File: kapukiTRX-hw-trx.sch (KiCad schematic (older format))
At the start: 28 parts, among them J1 GPS, J2 SWD, J21 Conn_01x01, J22 Conn_01x01, U1 STM32G474VE, U2 LP38693-3.3, Y1 16MHz

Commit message: Add an elec cap to cup rail
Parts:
- added C41: 10uF, Capacitor_Tantalum_SMD:CP_EIA-3216-18_Kemet-A, symbol Device:CP
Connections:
- wire segments 161 -> 165
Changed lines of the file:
@@
 	4950 6300 5150 6300
 Connection ~ 4950 6300
+$Comp
+L Device:CP C41
+U 1 1 5DCE2D86
+P 950 1000
+F 0 "C41" H 1068 1046 50  0000 L CNN
+F 1 "10uF" H 1068 955 50  0000 L CNN
+F 2 "Capacitor_Tantalum_SMD:CP_EIA-3216-18_Kemet-A" H 988 850 50  0001 C CNN
+F 3 "~" H 950 1000 50  0001 C CNN
+	1    950  1000
+	1    0    0    -1
+$EndComp
+Wire Wire Line
+	950  850  950  650
+Wire Wire Line
+	950  650  1400 650
+Connection ~ 1400 650
+Wire Wire Line
+	950  1150 950  1350
+Wire Wire Line
+	950  1350 1400 1350
 $EndSCHEMATC

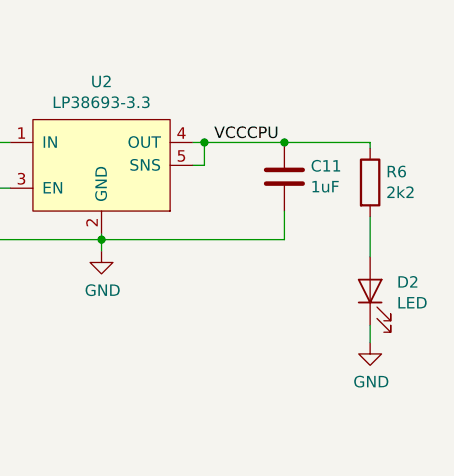
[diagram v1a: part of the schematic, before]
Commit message: Fix BMP388 footprint issue
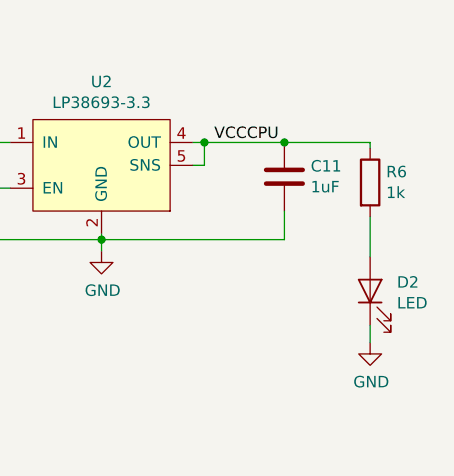
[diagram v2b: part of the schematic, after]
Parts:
- R6: value 2k2 -> 1k
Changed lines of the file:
@@
 EESchema Schematic File Version 4
+LIBS:kapukiTRX-hw-trx-cache
 EELAYER 30 0
 EELAYER END
@@
 P 10800 1275
 F 0 "R6" H 10870 1321 50  0000 L CNN
-F 1 "2k2" H 10870 1230 50  0000 L CNN
+F 1 "1k" H 10870 1230 50  0000 L CNN
 F 2 "Resistor_SMD:R_0402_1005Metric" V 10730 1275 50  0001 C CNN
 F 3 "~" H 10800 1275 50  0001 C CNN

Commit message: Final changes for rev.3
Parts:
- added R15: 0, Resistor_SMD:R_0402_1005Metric, symbol Device:R
- added R16: 10k, Resistor_SMD:R_0402_1005Metric, symbol Device:R
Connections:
- wire segments 165 -> 175
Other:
- note added: "CAN and servo interface"
- note added: "Extra serial port"
- note added: "GPS module connection"
- note added: "Main CPU"
- note added: "Redundant SX1280 RF modules (2.4 GHz)"
- note added: "SWD programming port"
- note added: "Sensors (9-axis absolute orientation sensor & pressure sensor for altitude measurement)"
- note added: "Status LED"
- note added: "Transmitter or receiver selection\nR15 mounter: transmitter\nR15 not mounted: receiver"
- moved on the sheet: C5, D1, J1, J2, J21, J22, R1, R14, R2, R3, R4

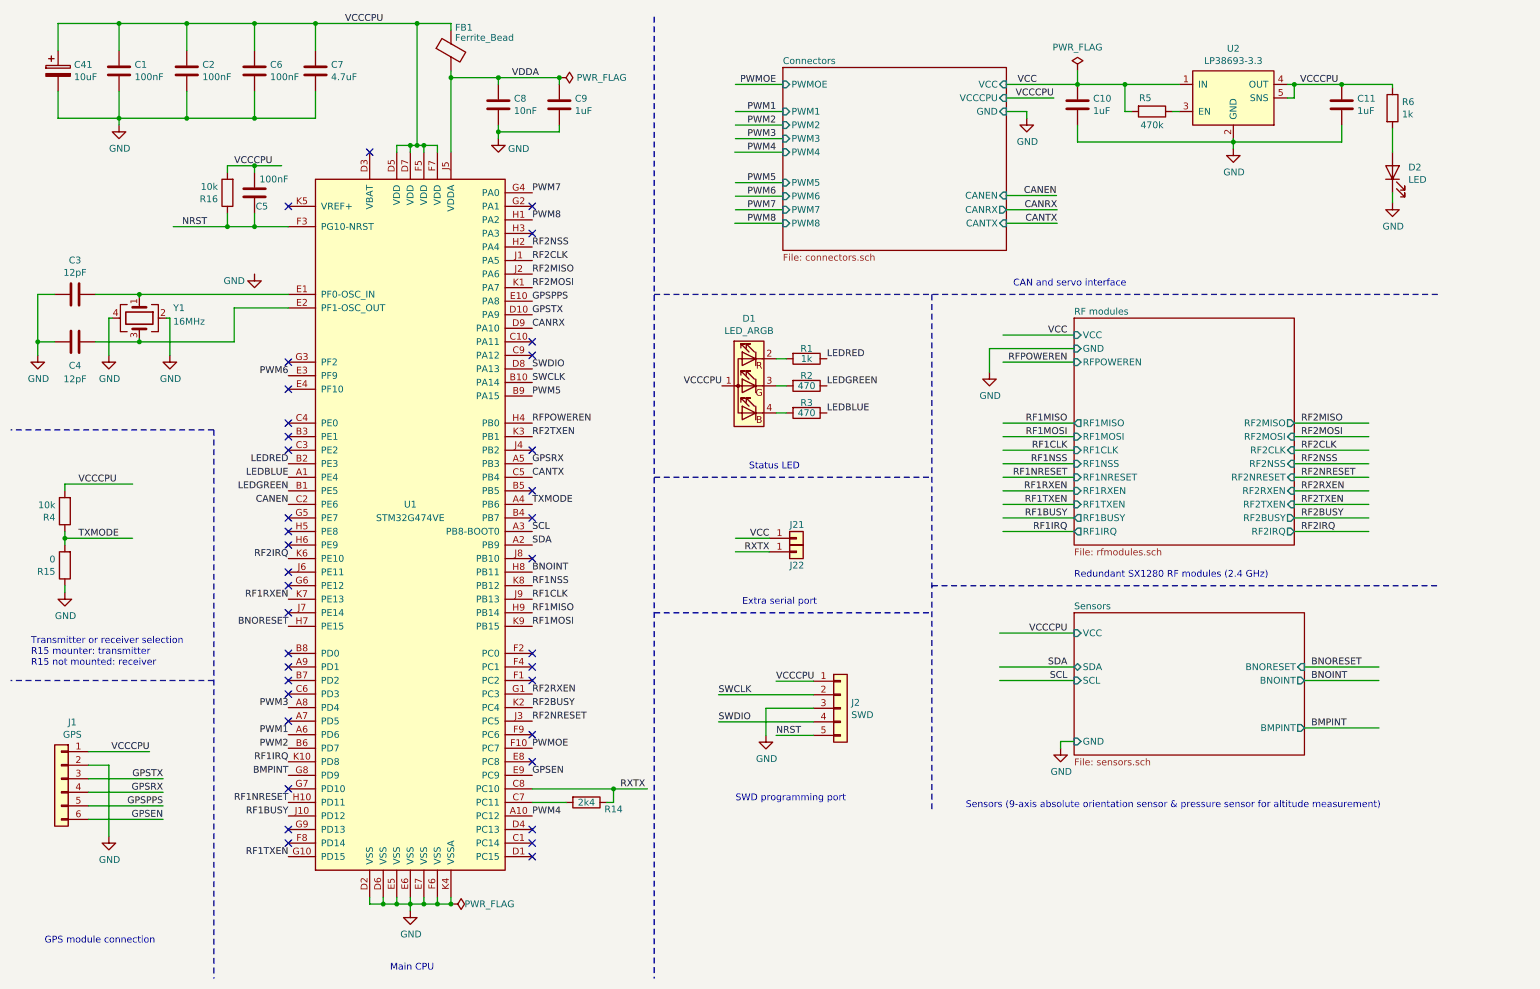
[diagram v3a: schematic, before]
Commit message: Add boot resistor, and fix CAN RX pin
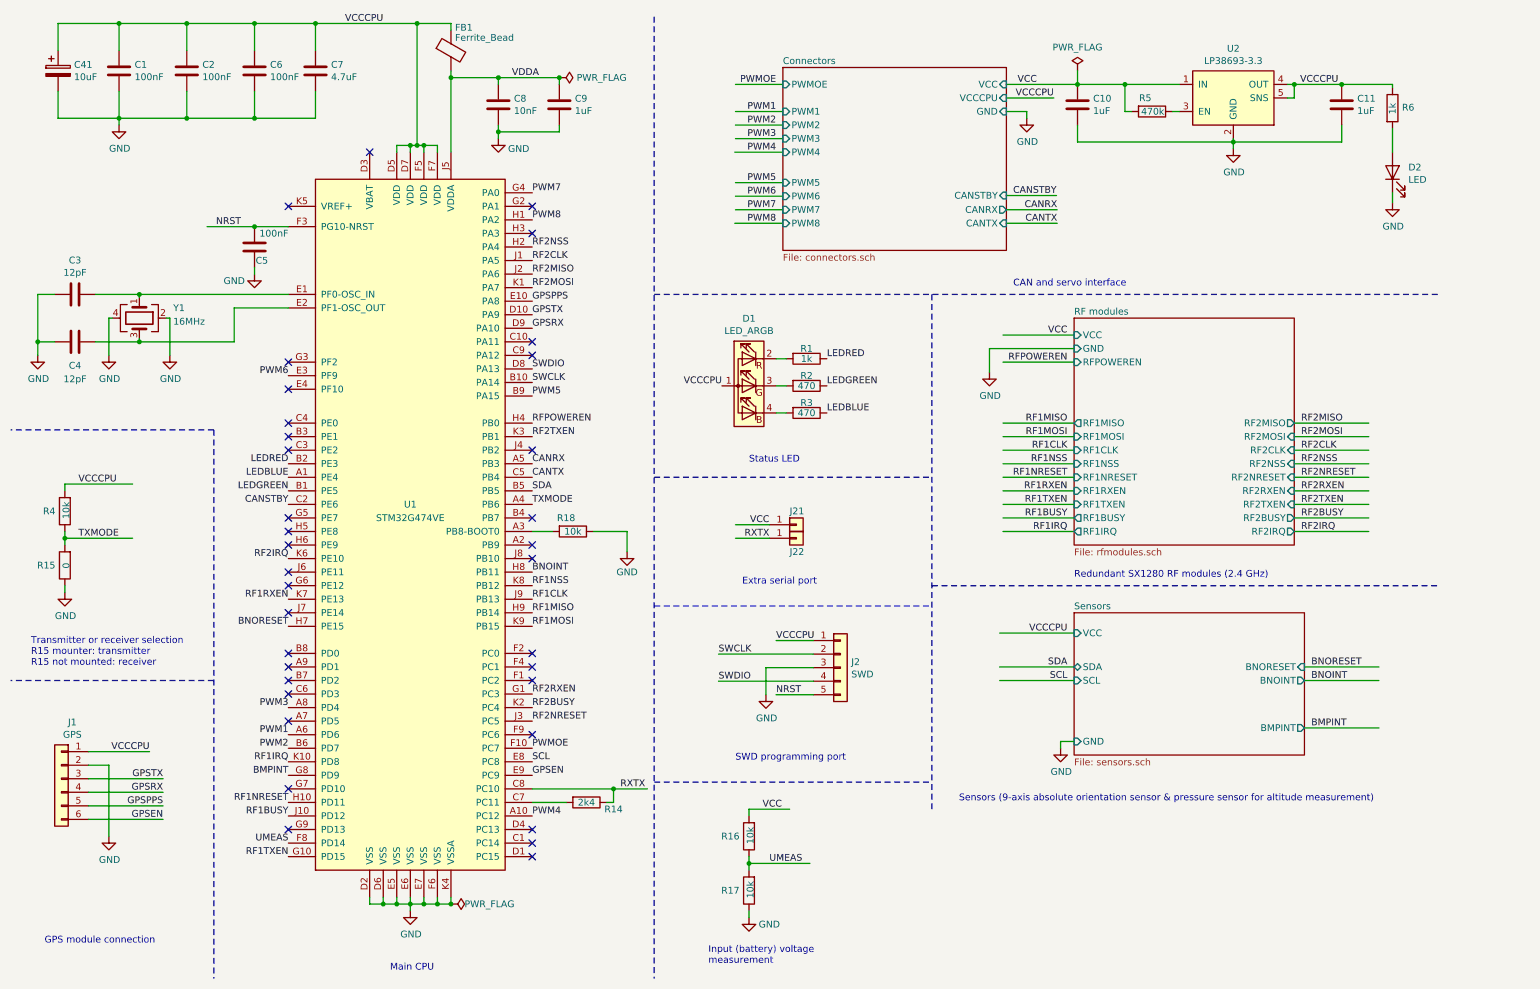
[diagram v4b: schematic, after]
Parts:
- added R17, R18: 10k, Resistor_SMD:R_0402_1005Metric, symbol Device:R
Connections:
- net labels added: CANSTBY, UMEAS
- net labels removed: CANEN
- wire segments 175 -> 178
- no-connect marks 37 -> 35
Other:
- note added: "Input (battery) voltage\nmeasurement"
- moved on the sheet: C5, J2, J21, J22
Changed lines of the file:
@@
 Sheet 1 4
 Title "kapukiTRX - transmitter & 8 channel receiver"
-Date "2020-01-01"
-Rev "3"
+Date "2020-03-29"
+Rev "4"
 Comp "bodrico.com"
 Comment1 "Designed by bodri@bodrico.com"
@@
 F14 "CANRX" O R 7950 2025 50
 F15 "CANTX" I R 7950 2125 50
-F16 "CANEN" I R 7950 1920 50
+F16 "CANSTBY" I R 7950 1920 50
 $EndSheet
-Text Label 5825 5605 0    50   ~ 0
+Text Label 5825 5305 0    50   ~ 0
 SWCLK
 Text Label 4450 5000 0    50   ~ 0
@@
 P 9025 1300
 F 0 "R5" V 8925 1250 50  0000 C CNN
-F 1 "470k" V 9125 1300 50  0000 C CNN
+F 1 "470k" V 9025 1305 50  0000 C CNN
 F 2 "Resistor_SMD:R_0402_1005Metric" V 8955 1300 50  0001 C CNN
 F 3 "~" H 9025 1300 50  0001 C CNN
@@
 RF2NSS
 Wire Wire Line
-	5825 5605 6525 5605
+	5825 5305 6525 5305
 $Comp
 L power:GND #PWR09
 U 1 1 5C88797A
-P 6175 5905
-F 0 "#PWR09" H 6175 5655 50  0001 C CNN
-F 1 "GND" H 6180 5732 50  0000 C CNN
-F 2 "" H 6175 5905 50  0001 C CNN
-F 3 "" H 6175 5905 50  0001 C CNN
-	1    6175 5905
-	1    0    0    -1
-$EndComp
-Wire Wire Line
-	6525 5505 6250 5505
-Text Label 6250 5505 0    50   ~ 0
+P 6175 5605
+F 0 "#PWR09" H 6175 5355 50  0001 C CNN
+F 1 "GND" H 6180 5432 50  0000 C CNN
+F 2 "" H 6175 5605 50  0001 C CNN
+F 3 "" H 6175 5605 50  0001 C CNN
+	1    6175 5605
+	1    0    0    -1
+$EndComp
+Wire Wire Line
+	6525 5205 6250 5205
+Text Label 6250 5205 0    50   ~ 0
 VCCCPU
 Text Label 6250 1100 2    50   ~ 0
@@
 RF2NSS
 Wire Wire Line
-	6175 5705 6525 5705
-Wire Wire Line
-	6175 5905 6175 5705
-Wire Wire Line
-	5825 5805 6525 5805
+	6175 5405 6525 5405
+Wire Wire Line
+	6175 5605 6175 5405
+Wire Wire Line
+	5825 5505 6525 5505
 $Comp
 L Connector_Generic:Conn_01x05 J2
 U 1 1 5CC22AC7
-P 6725 5705
-F 0 "J2" H 6805 5747 50  0000 L CNN
-F 1 "SWD" H 6805 5656 50  0000 L CNN
-F 2 "Connector_JST:JST_SH_BM05B-SRSS-TB_1x05-1MP_P1.00mm_Vertical" H 6725 5705 50  0001 C CNN
-F 3 "~" H 6725 5705 50  0001 C CNN
-	1    6725 5705
-	1    0    0    -1
-$EndComp
-Wire Wire Line
-	6525 5905 6250 5905
-Text Label 6250 5905 0    50   ~ 0
+P 6725 5405
+F 0 "J2" H 6805 5447 50  0000 L CNN
+F 1 "SWD" H 6805 5356 50  0000 L CNN
+F 2 "Connector_JST:JST_SH_BM05B-SRSS-TB_1x05-1MP_P1.00mm_Vertical" H 6725 5405 50  0001 C CNN
+F 3 "~" H 6725 5405 50  0001 C CNN
+	1    6725 5405
+	1    0    0    -1
+$EndComp
+Wire Wire Line
+	6525 5605 6250 5605
+Text Label 6250 5605 0    50   ~ 0
 NRST
-Text Label 2050 2150 2    50   ~ 0
+Text Label 2300 2150 2    50   ~ 0
 NRST
 $Comp
@@
 U 1 1 5CC4355B
 P 10800 1275
-F 0 "R6" H 10870 1321 50  0000 L CNN
-F 1 "1k" H 10870 1230 50  0000 L CNN
+F 0 "R6" H 10870 1280 50  0000 L CNN
+F 1 "1k" V 10800 1230 50  0000 L CNN
 F 2 "Resistor_SMD:R_0402_1005Metric" V 10730 1275 50  0001 C CNN
 F 3 "~" H 10800 1275 50  0001 C CNN
@@
 	0    1    1    0
 $EndComp
-Text Label 4450 2900 0    50   ~ 0
+Text Label 4450 3900 0    50   ~ 0
 CANRX
 Text Label 6250 1300 2    50   ~ 0
@@
 Wire Wire Line
 	6300 2125 5945 2125
-Text Label 5825 5805 0    50   ~ 0
+Text Label 5825 5505 0    50   ~ 0
 SWDIO
 Text Label 4450 3300 0    50   ~ 0
@@
 Text Label 2650 5700 2    50   ~ 0
 PWM3
-Text Label 4450 3900 0    50   ~ 0
+Text Label 4450 2900 0    50   ~ 0
 GPSRX
 Text Label 4450 2800 0    50   ~ 0
@@
 GPSEN
 Text Label 8320 1920 2    50   ~ 0
-CANEN
+CANSTBY
 Wire Wire Line
 	7950 1920 8320 1920
@@
 L Device:C C5
 U 1 1 5CF3CB0A
-P 2400 1900
-F 0 "C5" H 2300 2000 50  0000 L CNN
-F 1 "100nF" H 2150 1800 50  0000 L CNN
-F 2 "Capacitor_SMD:C_0402_1005Metric" H 2438 1750 50  0001 C CNN
-F 3 "~" H 2400 1900 50  0001 C CNN
-	1    2400 1900
+P 2400 2300
+F 0 "C5" H 2300 2400 50  0000 L CNN
+F 1 "100nF" H 2150 2200 50  0000 L CNN
+F 2 "Capacitor_SMD:C_0402_1005Metric" H 2438 2150 50  0001 C CNN
+F 3 "~" H 2400 2300 50  0001 C CNN
+	1    2400 2300
 	-1   0    0    1
 $EndComp
-Text Label 4450 4500 0    50   ~ 0
+Text Label 4450 4100 0    50   ~ 0
 SDA
-Text Label 4450 4400 0    50   ~ 0
+Text Label 4450 6100 0    50   ~ 0
 SCL
 Text Label 8400 5400 2    50   ~ 0
@@
 	10150 5850 10700 5850
 Text Label 2650 4200 2    50   ~ 0
-CANEN
+CANSTBY
 $Comp
 L Device:R R4
 U 1 1 5C7B6C85
 P 1000 4250
-F 0 "R4" H 1070 4296 50  0000 L CNN
-F 1 "10k" H 1070 4205 50  0000 L CNN
+F 0 "R4" H 1070 4250 50  0000 L CNN
+F 1 "10k" V 990 4180 50  0000 L CNN
 F 2 "Resistor_SMD:R_0402_1005Metric" V 930 4250 50  0001 C CNN
 F 3 "~" H 1000 4250 50  0001 C CNN
@@
 NoConn ~ 4450 2000
 NoConn ~ 4450 2200
-NoConn ~ 4450 4100
 NoConn ~ 2650 5800
 NoConn ~ 4450 4300
@@
 NoConn ~ 4450 5500
 NoConn ~ 4450 5900
-NoConn ~ 4450 6100
 NoConn ~ 4450 6600
 NoConn ~ 4450 6700
 NoConn ~ 4450 6800
-NoConn ~ 2650 6700
 NoConn ~ 2650 6600
 NoConn ~ 2650 3600
@@
 L Connector_Generic:Conn_01x01 J21
 U 1 1 5DC793B8
+P 6400 4350
+F 0 "J21" H 6350 4450 50  0000 L CNN
+F 1 "Conn_01x01" H 6480 4301 50  0001 L CNN
+F 2 "miscellaneous:PinHeader_1x01_P1.27mm" H 6400 4350 50  0001 C CNN
+F 3 "~" H 6400 4350 50  0001 C CNN
+	1    6400 4350
+	1    0    0    -1
+$EndComp
+$Comp
+L Connector_Generic:Conn_01x01 J22
+U 1 1 5DC79645
 P 6400 4450
-F 0 "J21" H 6350 4550 50  0000 L CNN
+F 0 "J22" H 6350 4350 50  0000 L CNN
 F 1 "Conn_01x01" H 6480 4401 50  0001 L CNN
 F 2 "miscellaneous:PinHeader_1x01_P1.27mm" H 6400 4450 50  0001 C CNN
@@
 	1    0    0    -1
 $EndComp
-$Comp
-L Connector_Generic:Conn_01x01 J22
-U 1 1 5DC79645
-P 6400 4550
-F 0 "J22" H 6350 4450 50  0000 L CNN
-F 1 "Conn_01x01" H 6480 4501 50  0001 L CNN
-F 2 "miscellaneous:PinHeader_1x01_P1.27mm" H 6400 4550 50  0001 C CNN
-F 3 "~" H 6400 4550 50  0001 C CNN
-	1    6400 4550
-	1    0    0    -1
-$EndComp
+Text Label 6200 4350 2    50   ~ 0
+VCC
 Text Label 6200 4450 2    50   ~ 0
-VCC
-Text Label 6200 4550 2    50   ~ 0
 RXTX
 Wire Wire Line
+	6200 4350 5950 4350
+Wire Wire Line
 	6200 4450 5950 4450
-Wire Wire Line
-	6200 4550 5950 4550
 $Comp
 L Device:R R14
@@
 U 1 1 5E18C312
 P 1000 4650
-F 0 "R15" H 1070 4696 50  0000 L CNN
-F 1 "0" H 1070 4605 50  0000 L CNN
+F 0 "R15" H 1070 4650 50  0000 L CNN
+F 1 "0" V 990 4630 50  0000 L CNN
 F 2 "Resistor_SMD:R_0402_1005Metric" V 930 4650 50  0001 C CNN
 F 3 "~" H 1000 4650 50  0001 C CNN
@@
 Wire Wire Line
 	1000 4100 1000 4050
-$Comp
-L Device:R R16
-U 1 1 5E1E5C91
-P 2200 1900
-F 0 "R16" H 2270 1946 50  0000 L CNN
-F 1 "10k" H 2270 1855 50  0000 L CNN
-F 2 "Resistor_SMD:R_0402_1005Metric" V 2130 1900 50  0001 C CNN
-F 3 "~" H 2200 1900 50  0001 C CNN
-	1    2200 1900
-	-1   0    0    1
-$EndComp
-Wire Wire Line
-	2400 2150 2400 2050
-Wire Wire Line
-	2400 2150 2200 2150
-Wire Wire Line
-	2200 2150 2200 2050
 Connection ~ 2400 2150
-Wire Wire Line
-	2200 2150 1800 2150
-Connection ~ 2200 2150
-Wire Wire Line
-	2200 1750 2200 1700
-Wire Wire Line
-	2200 1700 2400 1700
-Wire Wire Line
-	2400 1700 2400 1750
-Text Label 2250 1700 0    50   ~ 0
-VCCCPU
-Wire Wire Line
-	2400 1700 2600 1700
-Connection ~ 2400 1700
 Wire Notes Line
 	2100 3650 600  3650
@@
 Wire Notes Line
 	5350 4000 7400 4000
-Wire Notes Line
-	5350 5000 7400 5000
-Text Notes 6050 3950 0    50   ~ 0
+Text Notes 6050 3900 0    50   ~ 0
 Status LED
-Text Notes 6000 4950 0    50   ~ 0
+Text Notes 6000 4800 0    50   ~ 0
 Extra serial port
-Text Notes 5950 6400 0    50   ~ 0
+Text Notes 5950 6100 0    50   ~ 0
 SWD programming port
 Wire Notes Line
@@
 Text Notes 8450 4750 0    50   ~ 0
 Redundant SX1280 RF modules (2.4 GHz)
-Text Notes 7650 6450 0    50   ~ 0
+Text Notes 7600 6400 0    50   ~ 0
 Sensors (9-axis absolute orientation sensor & pressure sensor for altitude measurement)
 Text Notes 750  5400 0    50   ~ 0
@@
 Text Notes 3400 7650 0    50   ~ 0
 Main CPU
+Wire Wire Line
+	2050 2150 2400 2150
+Wire Wire Line
+	2400 2500 2400 2450
+$Comp
+L Device:R R16
+U 1 1 5E8841F2
+P 6050 6650
+F 0 "R16" H 6120 6650 50  0000 L CNN
+F 1 "10k" V 6040 6580 50  0000 L CNN
+F 2 "Resistor_SMD:R_0402_1005Metric" V 5980 6650 50  0001 C CNN
+F 3 "~" H 6050 6650 50  0001 C CNN
+	1    6050 6650
+	-1   0    0    1
+$EndComp
+$Comp
+L Device:R R17
+U 1 1 5E88472C
+P 6050 7050
+F 0 "R17" H 6120 7050 50  0000 L CNN
+F 1 "10k" V 6040 6980 50  0000 L CNN
+F 2 "Resistor_SMD:R_0402_1005Metric" V 5980 7050 50  0001 C CNN
+F 3 "~" H 6050 7050 50  0001 C CNN
+	1    6050 7050
+	-1   0    0    1
+$EndComp
+$Comp
+L power:GND #PWR030
+U 1 1 5E884936
+P 6050 7250
+F 0 "#PWR030" H 6050 7000 50  0001 C CNN
+F 1 "GND" H 6200 7200 50  0000 C CNN
+F 2 "" H 6050 7250 50  0001 C CNN
+F 3 "" H 6050 7250 50  0001 C CNN
+	1    6050 7250
+	1    0    0    -1
+$EndComp
+Wire Wire Line
+	6050 7250 6050 7200
+Wire Wire Line
+	6050 6900 6050 6850
+Text Label 6150 6450 0    50   ~ 0
+VCC
+Wire Wire Line
+	6050 6500 6050 6450
+Wire Wire Line
+	6050 6450 6350 6450
+Wire Wire Line
+	6050 6850 6500 6850
+Connection ~ 6050 6850
+Wire Wire Line
+	6050 6850 6050 6800
+Text Notes 5750 7600 0    50   ~ 0
+Input (battery) voltage\nmeasurement
+Wire Notes Line
+	5350 4950 7400 4950
+Wire Notes Line
+	5350 6250 7400 6250
+Text Label 6200 6850 0    50   ~ 0
+UMEAS
+Text Label 2650 6700 2    50   ~ 0
+UMEAS
+$Comp
+L Device:R R18
+U 1 1 5E907618
+P 4750 4400
+F 0 "R18" V 4650 4350 50  0000 C CNN
+F 1 "10k" V 4750 4400 50  0000 C CNN
+F 2 "Resistor_SMD:R_0402_1005Metric" V 4680 4400 50  0001 C CNN
+F 3 "~" H 4750 4400 50  0001 C CNN
+	1    4750 4400
+	0    1    1    0
+$EndComp
+$Comp
+L power:GND #PWR0113
+U 1 1 5E907CB8
+P 5150 4550
+F 0 "#PWR0113" H 5150 4300 50  0001 C CNN
+F 1 "GND" H 5150 4400 50  0000 C CNN
+F 2 "" H 5150 4550 50  0001 C CNN
+F 3 "" H 5150 4550 50  0001 C CNN
+	1    5150 4550
+	1    0    0    -1
+$EndComp
+Wire Wire Line
+	4450 4400 4600 4400
+Wire Wire Line
+	4900 4400 5150 4400
+Wire Wire Line
+	5150 4400 5150 4550
+NoConn ~ 4450 4500
 $EndSCHEMATC
